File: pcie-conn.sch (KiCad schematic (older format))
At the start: 22 parts, among them J2 1-2199230-6

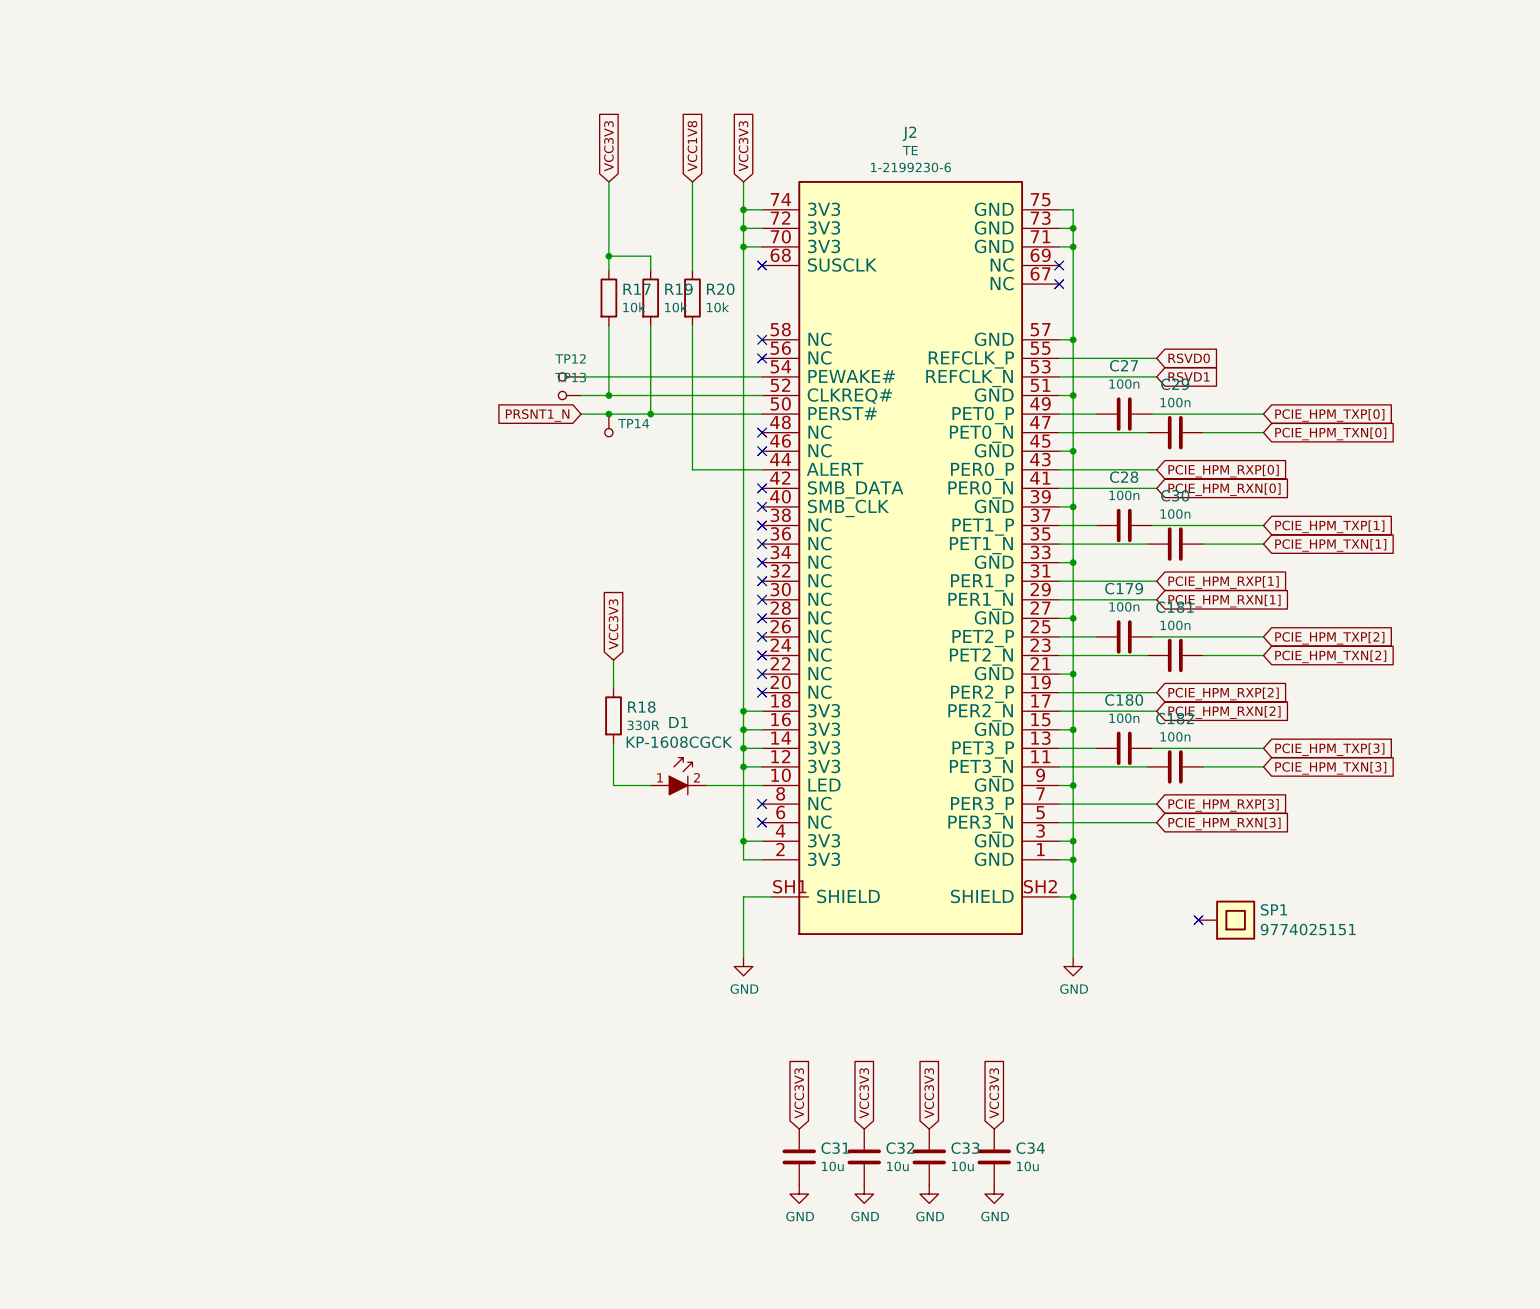
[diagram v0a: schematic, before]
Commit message: Clean M.2 sheet
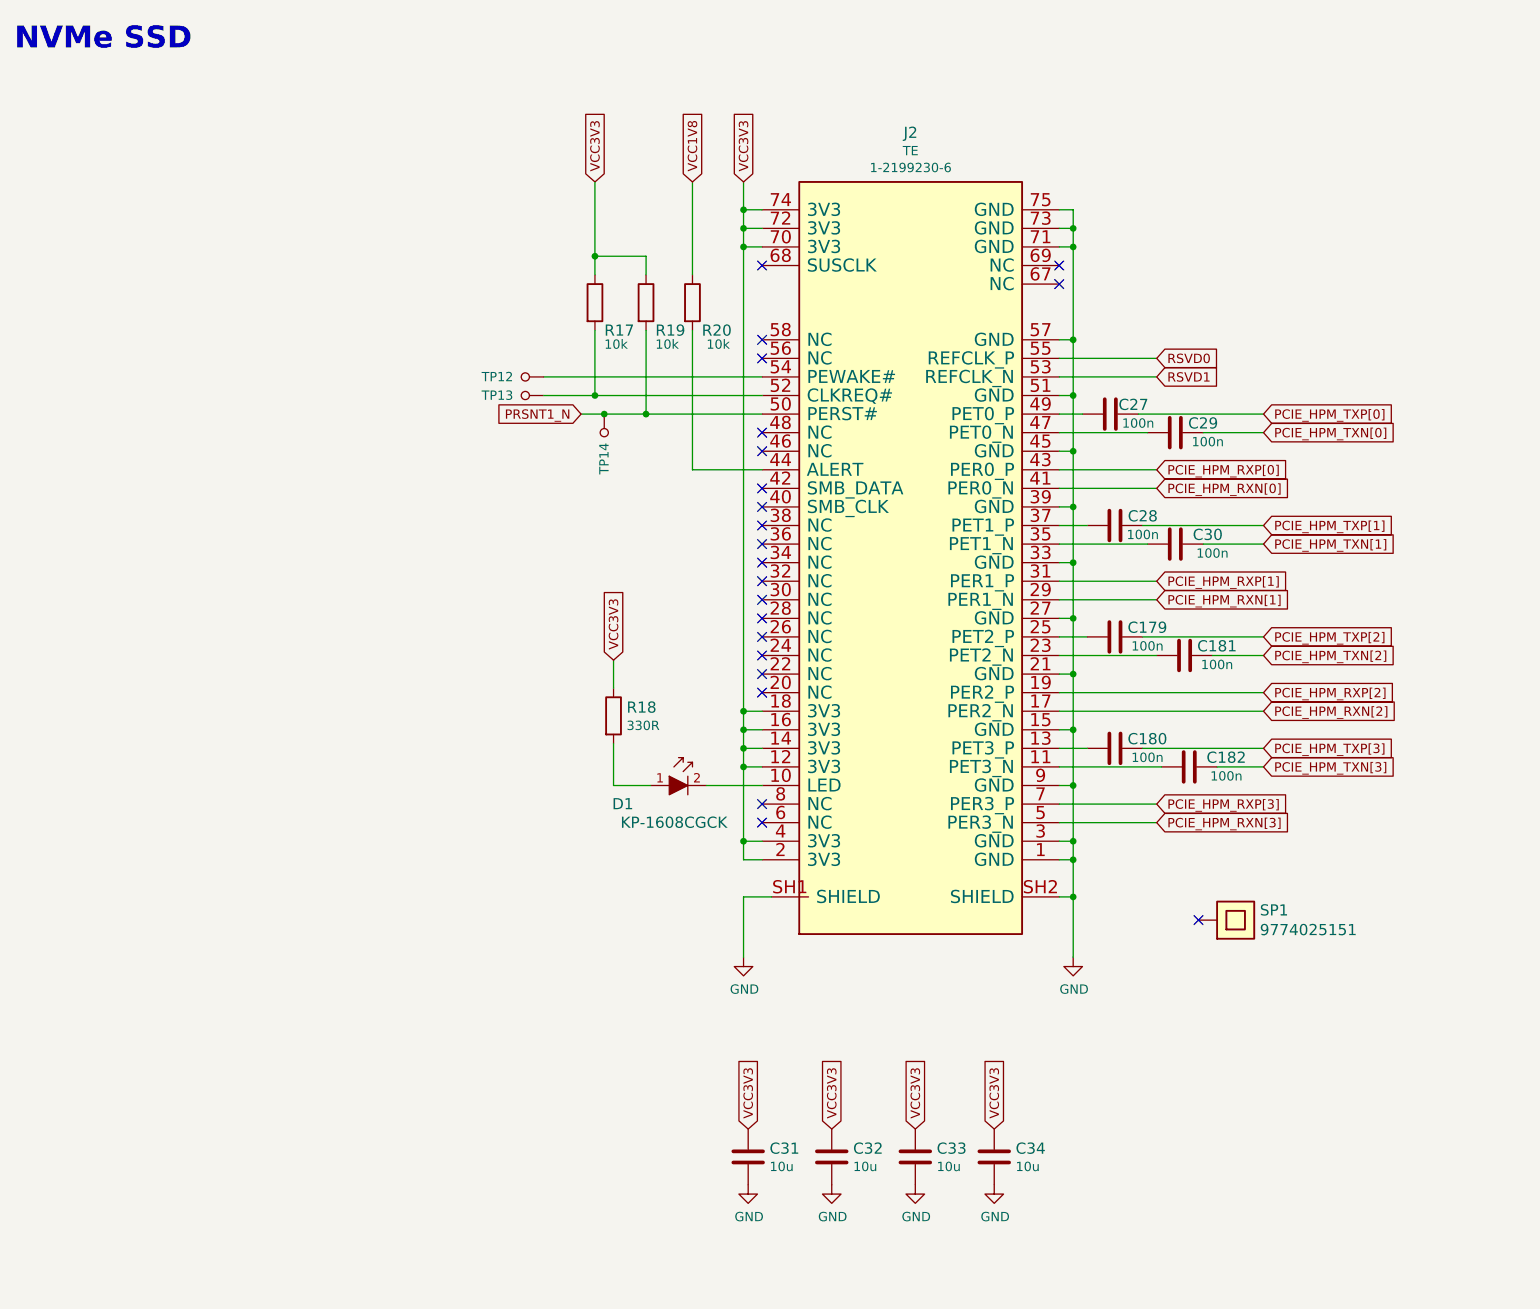
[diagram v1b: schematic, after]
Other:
- note added: "NVMe SSD"
- moved on the sheet: C179, C180, C181, C182, C27, C28, C31, C32, C33, R17, R19, R20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

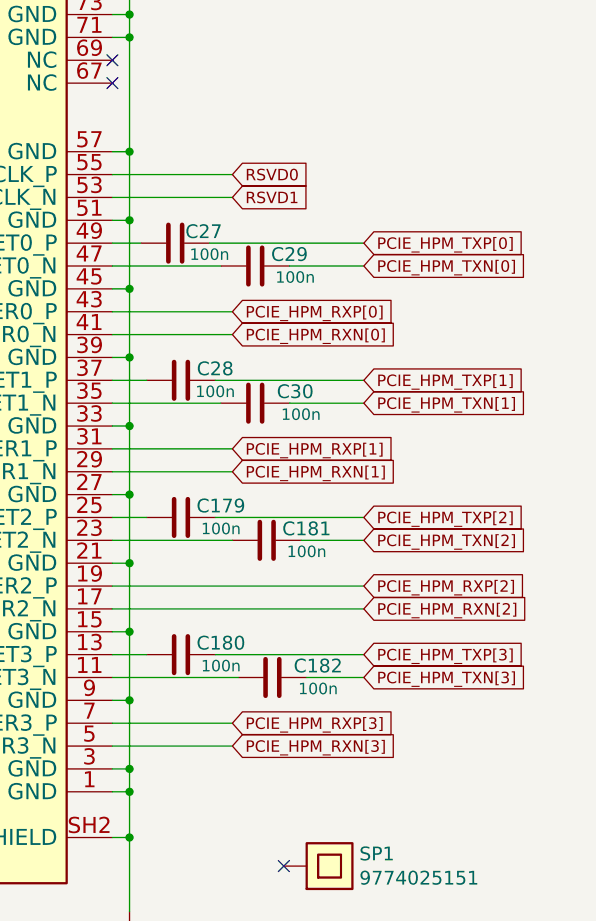
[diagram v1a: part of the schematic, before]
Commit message: Update naming convention for PCIe
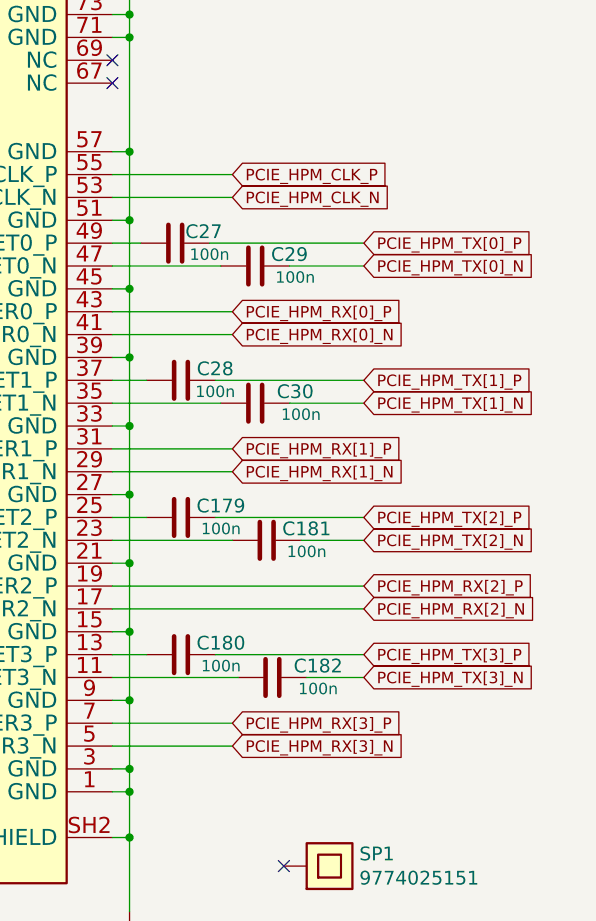
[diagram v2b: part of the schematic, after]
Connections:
- net PCIE_HPM_RXN[0] renamed PCIE_HPM_RX[0]_N
- net PCIE_HPM_RXN[1] renamed PCIE_HPM_RX[1]_N
- net PCIE_HPM_RXN[2] renamed PCIE_HPM_RX[2]_N
- net PCIE_HPM_RXN[3] renamed PCIE_HPM_RX[3]_N
- net PCIE_HPM_RXP[0] renamed PCIE_HPM_RX[0]_P
- net PCIE_HPM_RXP[1] renamed PCIE_HPM_RX[1]_P
- net PCIE_HPM_RXP[2] renamed PCIE_HPM_RX[2]_P
- net PCIE_HPM_RXP[3] renamed PCIE_HPM_RX[3]_P
- net PCIE_HPM_TXN[0] renamed PCIE_HPM_TX[0]_N
- net PCIE_HPM_TXN[1] renamed PCIE_HPM_TX[1]_N
- net PCIE_HPM_TXN[2] renamed PCIE_HPM_TX[2]_N
- net PCIE_HPM_TXN[3] renamed PCIE_HPM_TX[3]_N
- net PCIE_HPM_TXP[0] renamed PCIE_HPM_TX[0]_P
- net PCIE_HPM_TXP[1] renamed PCIE_HPM_TX[1]_P
- net PCIE_HPM_TXP[2] renamed PCIE_HPM_TX[2]_P
- net PCIE_HPM_TXP[3] renamed PCIE_HPM_TX[3]_P
- net RSVD0 renamed PCIE_HPM_CLK_P
- net RSVD1 renamed PCIE_HPM_CLK_N
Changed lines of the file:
@@
 NoConn ~ 6250 2050
 Text GLabel 6775 3050 2    50   Input ~ 0
-PCIE_HPM_RXP[0]
+PCIE_HPM_RX[0]_P
 Text GLabel 6775 3150 2    50   Input ~ 0
-PCIE_HPM_RXN[0]
+PCIE_HPM_RX[0]_N
 Text GLabel 7350 2750 2    50   Input ~ 0
-PCIE_HPM_TXP[0]
+PCIE_HPM_TX[0]_P
 Text GLabel 7350 2850 2    50   Input ~ 0
-PCIE_HPM_TXN[0]
+PCIE_HPM_TX[0]_N
 Text GLabel 6775 3650 2    50   Input ~ 0
-PCIE_HPM_RXP[1]
+PCIE_HPM_RX[1]_P
 Text GLabel 6775 3750 2    50   Input ~ 0
-PCIE_HPM_RXN[1]
+PCIE_HPM_RX[1]_N
 Text GLabel 6775 4850 2    50   Input ~ 0
-PCIE_HPM_RXP[3]
+PCIE_HPM_RX[3]_P
 Text GLabel 6775 4950 2    50   Input ~ 0
-PCIE_HPM_RXN[3]
+PCIE_HPM_RX[3]_N
 Text GLabel 7350 3350 2    50   Input ~ 0
-PCIE_HPM_TXP[1]
+PCIE_HPM_TX[1]_P
 Text GLabel 7350 3450 2    50   Input ~ 0
-PCIE_HPM_TXN[1]
+PCIE_HPM_TX[1]_N
 Text GLabel 7350 3950 2    50   Input ~ 0
-PCIE_HPM_TXP[2]
+PCIE_HPM_TX[2]_P
 Text GLabel 7350 4050 2    50   Input ~ 0
-PCIE_HPM_TXN[2]
+PCIE_HPM_TX[2]_N
 Text GLabel 7350 4550 2    50   Input ~ 0
-PCIE_HPM_TXP[3]
+PCIE_HPM_TX[3]_P
 Text GLabel 7350 4650 2    50   Input ~ 0
-PCIE_HPM_TXN[3]
+PCIE_HPM_TX[3]_N
 Wire Wire Line
 	6250 3950 6400 3950
@@
 	7075 4050 7350 4050
 Text GLabel 7350 4350 2    50   Input ~ 0
-PCIE_HPM_RXN[2]
+PCIE_HPM_RX[2]_N
 Text GLabel 7350 4250 2    50   Input ~ 0
-PCIE_HPM_RXP[2]
+PCIE_HPM_RX[2]_P
 Wire Wire Line
 	7350 4250 6250 4250
@@
 	7100 4650 7350 4650
 Text GLabel 6775 2450 2    50   Input ~ 0
-RSVD0
+PCIE_HPM_CLK_P
 Text GLabel 6775 2550 2    50   Input ~ 0
-RSVD1
+PCIE_HPM_CLK_N
 Text GLabel 3675 2750 0    50   Input ~ 0
 PRSNT1_N

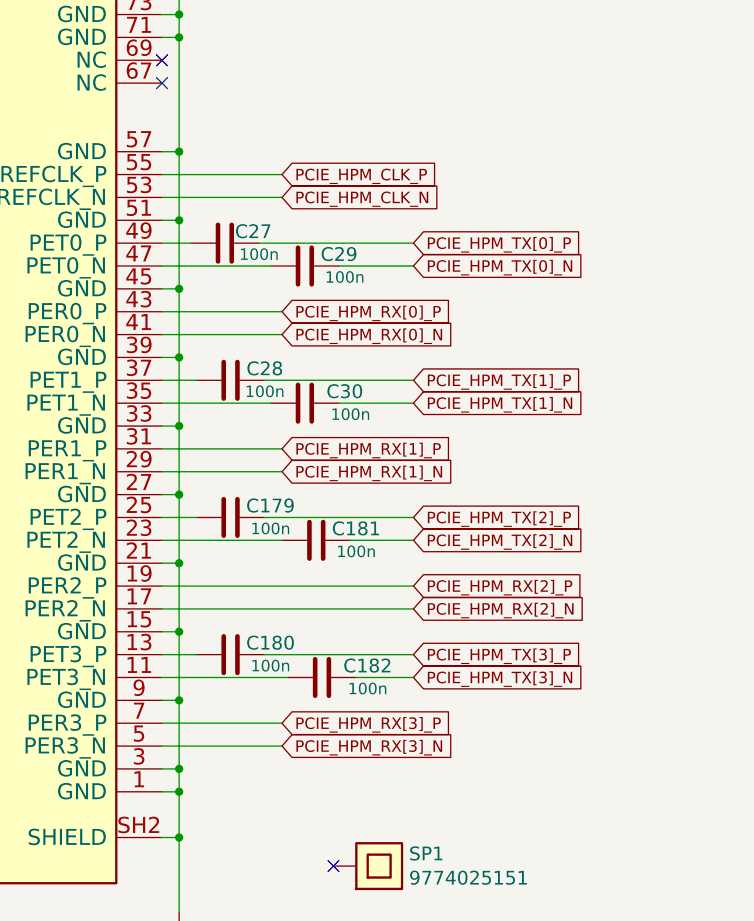
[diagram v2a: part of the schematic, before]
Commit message: Add net labels to coupled PCIe lanes
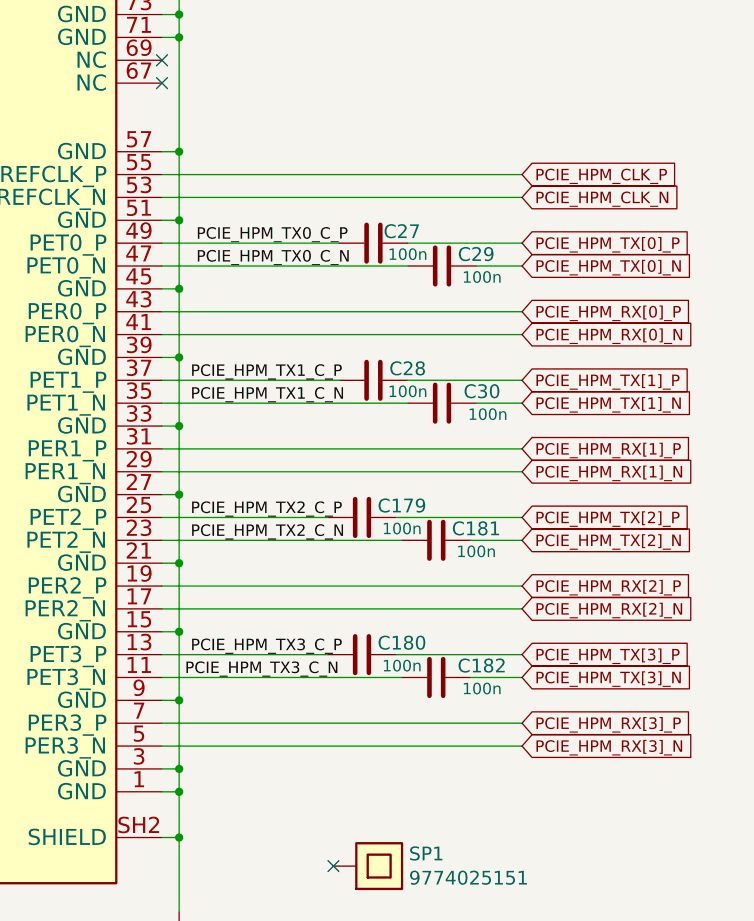
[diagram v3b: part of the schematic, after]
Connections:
- net PCIE_HPM_TX0_C_P: now reaches C27.1, J2.49 (PET0_P)
- net PCIE_HPM_TX0_C_N: now reaches C29.1, J2.47 (PET0_N)
- net PCIE_HPM_TX1_C_P: now reaches C28.1, J2.37 (PET1_P)
- net PCIE_HPM_TX1_C_N: now reaches C30.1, J2.35 (PET1_N)
- net PCIE_HPM_TX3_C_N: now reaches C182.1, J2.11 (PET3_N)
- net PCIE_HPM_TX3_C_P: now reaches C180.1, J2.13 (PET3_P)
- net PCIE_HPM_TX2_C_N: now reaches C181.1, J2.23 (PET2_N)
- net PCIE_HPM_TX2_C_P: now reaches C179.1, J2.25 (PET2_P)
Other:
- moved on the sheet: C179, C180, C181, C182, C27, C28, C29, C30

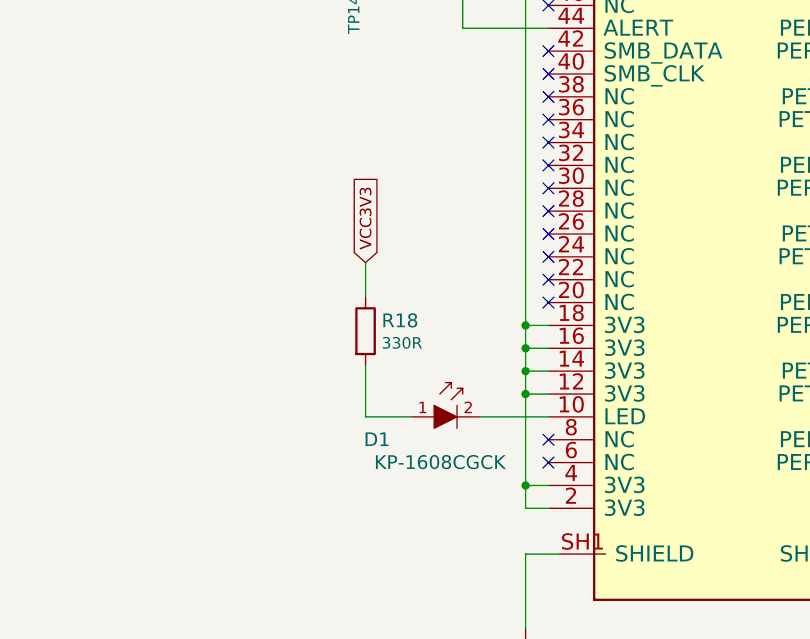
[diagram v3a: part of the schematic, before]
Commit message: Update schematic notes, update SPI0 connection
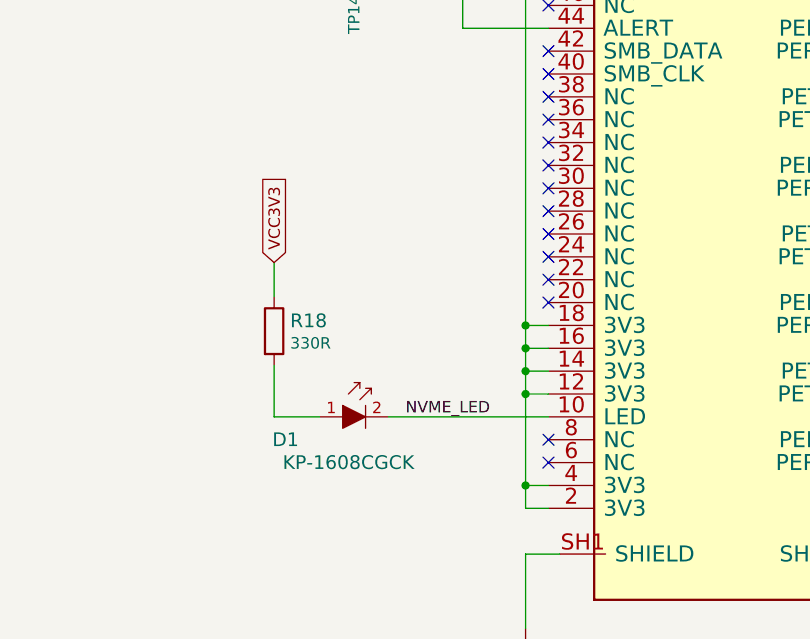
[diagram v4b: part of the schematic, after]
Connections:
- net NVME_LED: now reaches D1.2, J2.10 (LED)
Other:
- moved on the sheet: D1, R18
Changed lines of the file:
@@
 L artix-dc-scm:KP-1608CGCK D1
 U 1 1 5FD7D8E8
-P 4250 4750
-F 0 "D1" H 3900 4650 60  0000 C CNN
-F 1 "KP-1608CGCK" H 4175 4550 60  0000 C CNN
-F 2 "artix-dc-scm-footprints:LED_0603" H 4450 4950 60  0001 L CNN
-F 3 "http://www.farnell.com/datasheets/2045956.pdf" H 4450 5050 60  0001 L CNN
-F 4 "KP-1608CGCK" H 4450 5250 60  0001 L CNN "MPN"
-F 5 "KINGBRIGHT" H 4460 5370 60  0001 L CNN "Manufacturer"
-	1    4250 4750
-	1    0    0    -1
-$EndComp
-Wire Wire Line
-	4350 4750 4650 4750
+P 3850 4750
+F 0 "D1" H 3500 4650 60  0000 C CNN
+F 1 "KP-1608CGCK" H 3775 4550 60  0000 C CNN
+F 2 "artix-dc-scm-footprints:LED_0603" H 4050 4950 60  0001 L CNN
+F 3 "http://www.farnell.com/datasheets/2045956.pdf" H 4050 5050 60  0001 L CNN
+F 4 "KP-1608CGCK" H 4050 5250 60  0001 L CNN "MPN"
+F 5 "KINGBRIGHT" H 4060 5370 60  0001 L CNN "Manufacturer"
+	1    3850 4750
+	1    0    0    -1
+$EndComp
+Wire Wire Line
+	3950 4750 4650 4750
 $Comp
 L artix-dc-scm:R_330R_0402 R18
 U 1 1 5FD7EE61
-P 3850 4375
-F 0 "R18" V 3805 4445 60  0000 L CNN
-F 1 "R_330R_0402" H 3850 4225 60  0001 C CNN
-F 2 "artix-dc-scm-footprints:0402-res" H 4050 4575 60  0001 L CNN
-F 3 "" H 3850 4375 50  0001 C CNN
-F 4 "MULTICOMP" H 4050 4775 60  0001 L CNN "Manufacturer"
-F 5 "MCMR04X3300FTL" H 4050 4675 60  0001 L CNN "MPN"
-F 6 "330R" V 3903 4445 50  0000 L CNN "Val"
-	1    3850 4375
+P 3450 4375
+F 0 "R18" V 3405 4445 60  0000 L CNN
+F 1 "R_330R_0402" H 3450 4225 60  0001 C CNN
+F 2 "artix-dc-scm-footprints:0402-res" H 3650 4575 60  0001 L CNN
+F 3 "" H 3450 4375 50  0001 C CNN
+F 4 "MULTICOMP" H 3650 4775 60  0001 L CNN "Manufacturer"
+F 5 "MCMR04X3300FTL" H 3650 4675 60  0001 L CNN "MPN"
+F 6 "330R" V 3503 4445 50  0000 L CNN "Val"
+	1    3450 4375
 	0    1    1    0
 $EndComp
 Wire Wire Line
-	3850 4525 3850 4750
-Wire Wire Line
-	3850 4750 4050 4750
-Wire Wire Line
-	3850 4225 3850 4075
-Text GLabel 3850 4075 1    50   Input ~ 0
+	3450 4525 3450 4750
+Wire Wire Line
+	3450 4750 3650 4750
+Wire Wire Line
+	3450 4225 3450 4075
+Text GLabel 3450 4075 1    50   Input ~ 0
 VCC3V3
 Wire Wire Line
@@
 Text Label 6375 4550 0    50   ~ 0
 PCIE_HPM_TX3_C_P
+Text Label 4025 4750 0    50   ~ 0
+NVME_LED
 $EndSCHEMATC

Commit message: Fix USB3300 circuit
-remove 1V8 connection
-add capacitance at internal 1v8 regulators
-apply changes to PCB
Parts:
- C179, C180, C181, C182, C27, C28, C29, C30: footprint artix-dc-scm-footprints:0402-cap -> _autosave-artix-dc-scm-footprints:0402-cap; symbol artix-dc-scm:C_100n_0402-artix-dc-scm -> _autosave-artix-dc-scm:C_100n_0402-artix-dc-scm
- C31, C32, C33, C34: footprint artix-dc-scm-footprints:0402-cap -> _autosave-artix-dc-scm-footprints:0402-cap; symbol artix-dc-scm:C_10u_0402 -> _autosave-artix-dc-scm:C_10u_0402
- D1: footprint artix-dc-scm-footprints:LED_0603 -> _autosave-artix-dc-scm-footprints:LED_0603; symbol artix-dc-scm:KP-1608CGCK -> _autosave-artix-dc-scm:KP-1608CGCK
- J2: footprint artix-dc-scm-footprints:1-2199230-6 -> _autosave-artix-dc-scm-footprints:1-2199230-6; symbol artix-dc-scm:1-2199230-6 -> _autosave-artix-dc-scm:1-2199230-6
- R17, R19, R20: footprint artix-dc-scm-footprints:0402-res -> _autosave-artix-dc-scm-footprints:0402-res; symbol artix-dc-scm:R_10k_0402 -> _autosave-artix-dc-scm:R_10k_0402
- R18: footprint artix-dc-scm-footprints:0402-res -> _autosave-artix-dc-scm-footprints:0402-res; symbol artix-dc-scm:R_330R_0402 -> _autosave-artix-dc-scm:R_330R_0402
- SP1: footprint artix-dc-scm-footprints:9774025151 -> _autosave-artix-dc-scm-footprints:9774025151; symbol artix-dc-scm:9774025151 -> _autosave-artix-dc-scm:9774025151
- TP12, TP13, TP14: footprint artix-dc-scm-footprints:Testpoint_smd_1mm -> _autosave-artix-dc-scm-footprints:Testpoint_smd_1mm; symbol artix-dc-scm:TP_SMD1MM -> _autosave-artix-dc-scm:TP_SMD1MM
